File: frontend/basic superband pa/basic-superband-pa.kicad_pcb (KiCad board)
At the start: 2 copper layers, 64.5 x 60 mm, 73 parts, among them CN1 EDGE, K1 D3002, K2 D3002, P1 BNC, P2 CONN_02X01, Q1 NPN, Q2 PNP, Q3 RD16HHF1, T1 TRANSFO, T2 8:1, T3 4:1, T4 OUT_TRANSF, U1 LP2951-50D

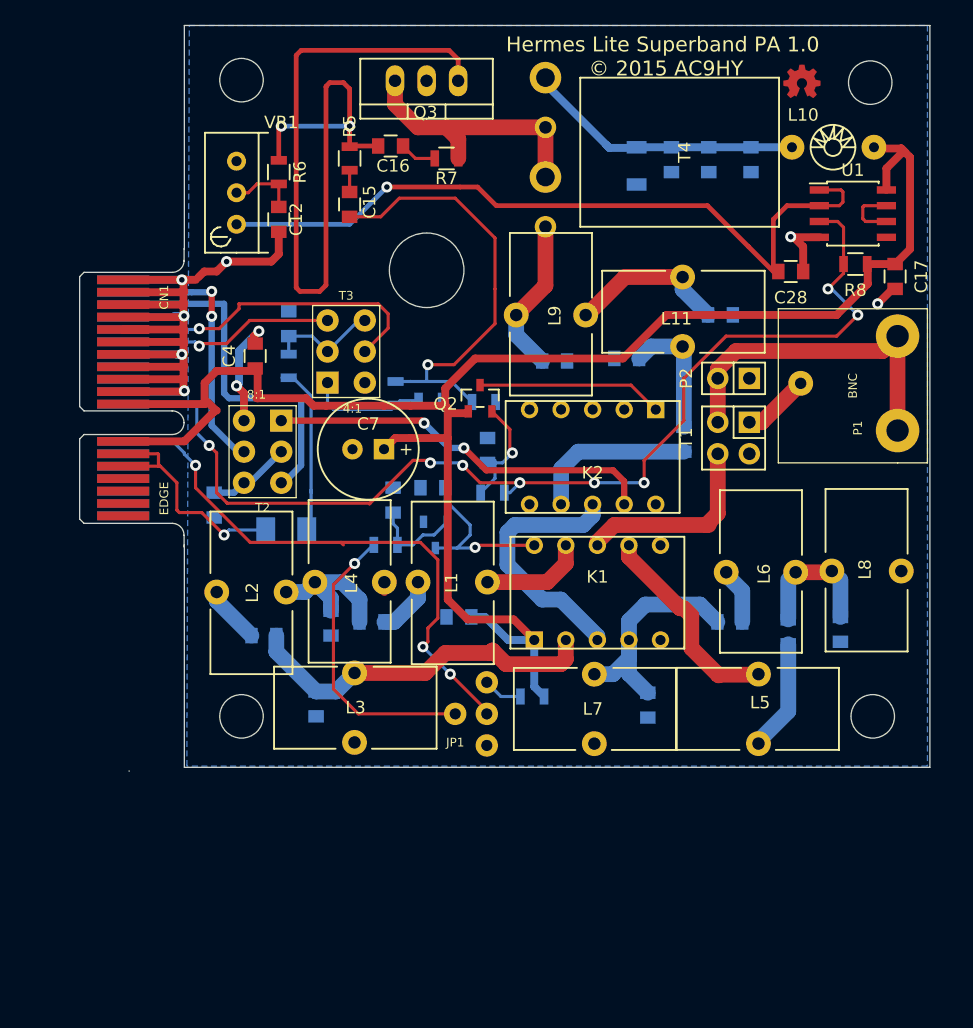
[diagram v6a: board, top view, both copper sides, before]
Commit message: PTT change
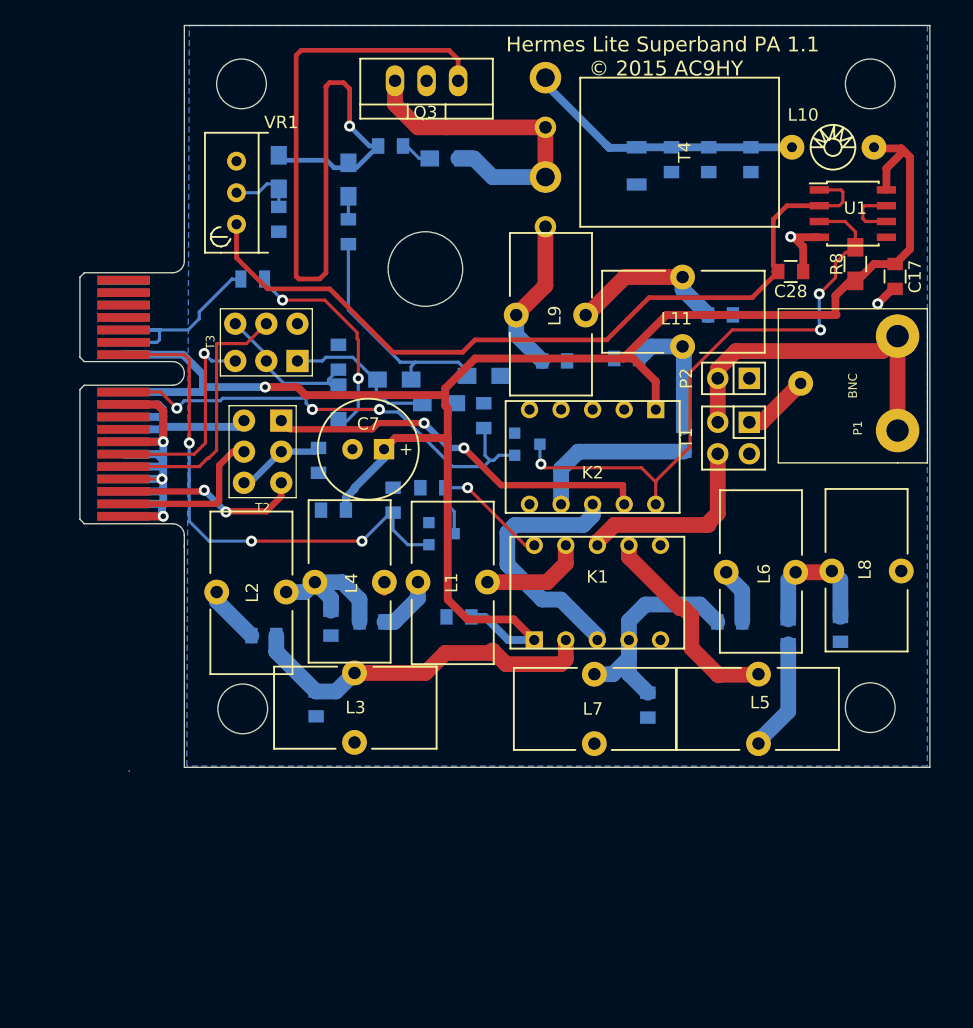
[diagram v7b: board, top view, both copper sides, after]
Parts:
- removed G***: OSHW-logo_copper-front_3mm, OSHW:OSHW-logo_copper-front_3mm
- removed JP1: JUMPER4, HERMESLITE:JUMPER4
- removed MountingHole_3-5mm (x4): VAL**, Mounting_Holes:MountingHole_3-5mm
- removed R1, R13: 4.99k, HERMESLITE:R_0805
- removed R2: 1k, HERMESLITE:R_0805
- added MountingHole_4mm: VAL**, Mounting_Holes:MountingHole_4mm, F.Cu at (189.6, 39.7)
- added MountingHole_4mm: VAL**, Mounting_Holes:MountingHole_4mm, F.Cu at (139.0, 39.7)
- added MountingHole_4mm: VAL**, Mounting_Holes:MountingHole_4mm, F.Cu at (139.1, 90.0)
- added MountingHole_4mm: VAL**, Mounting_Holes:MountingHole_4mm, F.Cu at (189.6, 89.9)
- C1: value 0.1uF -> 0.01uF
- C12, C15, C16, C4, CN1: moved to B.Cu
- FB1: footprint SMD_Packages:SMD-1206 -> SMD_Packages:SMD-0805
- Q1: value NPN -> FDV301; footprint Transistors_SMD:sot23 -> SMD_Packages:SOT-23-GDS
- Q2: value PNP -> FDV301; footprint Transistors_SMD:sot23 -> SMD_Packages:SOT-23-GDS; moved to B.Cu
- R10, R11, R12, R4, R8: footprint HERMESLITE:R_0805 -> Resistors_SMD:R_0805_HandSoldering
- R5, R6, R7: footprint HERMESLITE:R_0805 -> Resistors_SMD:R_0805_HandSoldering; moved to B.Cu
- moved FB1 20.4 mm to (139.9, 55.4)
- moved C4 13.9 mm to (146.4, 74.0), turned to 180 degrees
- moved C2 9.14 mm to (145.2, 70.0)
- moved Q2 5.30 mm to (162.0, 68.7), turned to 270 degrees
- moved R4 5.06 mm to (146.8, 65.5)
- moved C3 4.83 mm to (146.8, 61.7)
- moved CN1 3.97 mm to (126.0, 63.0), turned to 90 degrees
- moved T3 2.98 mm to (143.5, 62.0), turned to 90 degrees
- moved C1 2.82 mm to (158.5, 66.4)
- moved C15 2.20 mm to (147.6, 51.6)
- moved R12 2.10 mm to (158.5, 63.2)
- moved R5 1.70 mm to (147.6, 47.4)
- moved R11 1.10 mm to (151.3, 63.5), turned to 180 degrees
- moved R10 0.73 mm to (154.9, 65.4)
- moved Q1 0.51 mm to (155.1, 75.9), turned to 270 degrees
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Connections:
- C1 pad 1: Net-(C1-Pad1) -> PTT
- C25 pad 2: Net-(C25-Pad2) -> GPIO0
- CN1 pad B11: PTT# -> PTT
- K2 pad 1: Net-(K2-Pad1) -> Net-(C17-Pad1)
- K2 pad 10: GND -> /PTT
- R8 pad 1: Net-(C17-Pad1) -> /PTT
- R8 pad 2: PTT# -> Net-(C17-Pad1)
- U1 pad 3: PTT# -> /PTT
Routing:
- net PTT#: track 89.3 -> 0.00 mm, vias 8 -> 0
- net /PTT: track 0.00 -> 48.1 mm, vias 0 -> 3
- net PTT: track 0.00 -> 38.2 mm, vias 0 -> 3
- net GND: track 107.7 -> 73.4 mm, vias 9 -> 5
- net Net-(JP1-Pad2): track 23.6 -> 0.00 mm, vias 1 -> 0
- net Net-(C15-Pad2): track 35.5 -> 19.6 mm, vias 1 -> 0
- net Net-(K2-Pad1): track 15.0 -> 0.00 mm
- net Net-(CN1-PadB3): track 29.4 -> 15.2 mm, vias 0 -> 2
- net Net-(C1-Pad1): track 9.43 -> 0.00 mm, vias 1 -> 0
- net Net-(CN1-PadB2): track 21.6 -> 13.1 mm, vias 2 -> 0
- net Net-(C25-Pad2): track 7.52 -> 0.00 mm
- net Net-(CN1-PadB5): track 26.8 -> 21.4 mm, vias 1 -> 0
- net Net-(C28-Pad2): track 61.0 -> 65.9 mm, vias 1 -> 0
- net Net-(Q3-Pad3): track 21.7 -> 26.4 mm
- net GPIO0: track 45.7 -> 41.5 mm
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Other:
- board text added: "Hermes Lite Superband PA 1.1 © 2015 AC9HY"
- board text removed: "Hermes Lite Superband PA 1.0 © 2015 AC9HY"

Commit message: Added opto and change of PTT
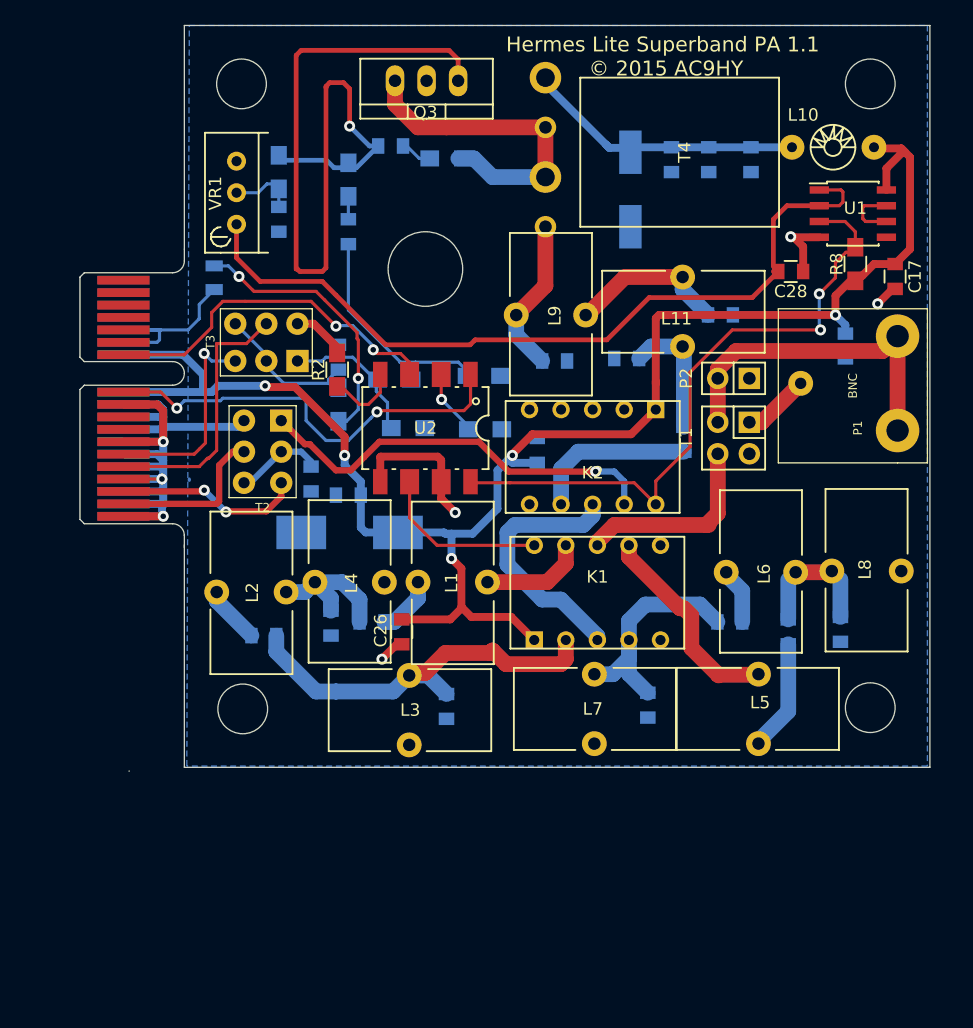
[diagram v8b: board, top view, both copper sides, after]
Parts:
- removed C1, C25, C27: 0.01uF, HERMESLITE:C_0805
- removed Q1, Q2: FDV301, SMD_Packages:SOT-23-GDS
- added C30: 0.1uF, HERMESLITE:C_0805, B.Cu at (187.6, 60.8)
- added C31: 0.1uF, HERMESLITE:C_0805, B.Cu at (162.8, 69.2)
- added R1: 1.2k, Resistors_SMD:R_0805_HandSoldering, B.Cu at (158.6, 67.5)
- added R2: 1.2k, Resistors_SMD:R_0805_HandSoldering, F.Cu at (146.7, 62.7)
- added U2: LVT827, Power_Integrations:SMD-8, F.Cu at (153.8, 67.4)
- C22: footprint Capacitors_SMD:C_1206 -> Capacitors_Tantalum_SMD:TantalC_SizeC_EIA-6032_HandSoldering
- C26: moved to F.Cu
- C7: footprint Discret:C1V8 -> Capacitors_Tantalum_SMD:TantalC_SizeD_EIA-7343_HandSoldering; moved to B.Cu
- moved C9 10.5 mm to (155.5, 89.8)
- moved C7 6.87 mm to (147.7, 75.8)
- moved C26 4.75 mm to (151.9, 83.8), turned to 90 degrees
- moved L3 4.40 mm to (159.1, 86.8)
- moved R10 3.20 mm to (152.4, 67.4)
- moved FB1 3.10 mm to (136.8, 55.3), turned to 90 degrees
- moved C22 1.96 mm to (170.3, 48.2)
- moved C4 1.70 mm to (147.6, 72.8)
- moved C2 1.62 mm to (144.6, 71.5)
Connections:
- CN1 pad B12: GPIO0 -> USEROUT0
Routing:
- net GPIO0: track 41.5 -> 0.00 mm, vias 3 -> 0
- net USEROUT0: track 0.00 -> 28.7 mm, vias 0 -> 2
- net GND: track 73.4 -> 90.9 mm, vias 5 -> 7
- net Net-(C17-Pad1): track 141.7 -> 135.6 mm, vias 1 -> 5
- net Net-(R2-Pad1): track 0.00 -> 5.92 mm
- net Net-(R1-Pad1): track 0.00 -> 5.32 mm, vias 0 -> 1
- net Net-(FB1-Pad2): track 17.6 -> 22.0 mm
- net /PTT: track 48.1 -> 52.2 mm, vias 3 -> 2
- net Net-(C6-Pad2): track 29.5 -> 33.1 mm
- net PTT: track 38.2 -> 35.0 mm, vias 3 -> 2
- net Net-(CN1-PadA13): track 18.3 -> 16.1 mm
- net Net-(K2-Pad9): track 31.6 -> 33.4 mm, vias 2 -> 1
- net Net-(C16-Pad2): track 67.9 -> 66.8 mm
- net Net-(R10-Pad2): track 12.6 -> 11.6 mm
- net Net-(K1-Pad10): track 13.1 -> 13.9 mm, vias 1 -> 0
